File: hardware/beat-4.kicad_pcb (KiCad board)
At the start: 4 copper layers, 70 x 70 mm, 109 parts, among them J1001 SJ2-25404B-SMT-TR, J101 Cortex, J102 DX07S016JA3, J201 DX07S016JA3, J202 KitProg3, J401 WAGO 2601-1101, J402 WAGO 2601-1101, J403 WAGO 2601-1101, J404 WAGO 2601-1101, J405 WAGO 2601-1101, J406 WAGO 2601-1101, J407 WAGO 2601-1101, J408 WAGO 2601-1101, Q201 BSC010N04LS, Q202 BSC010N04LS, Q601 BSC010N04LS, Q701 BSC010N04LS, Q801 BSC010N04LS, Q901 BSC010N04LS, SW101 SKSG, SW102 SKSG, U1001 TLP2361, U101 ATSAMD51G, U102 TPS78433QWDRBRQ1, U201 CYPM1311-48LDXI, U301 TPSM33620S5QRDNRQ1, U501 BTT6010, Y101 32k768

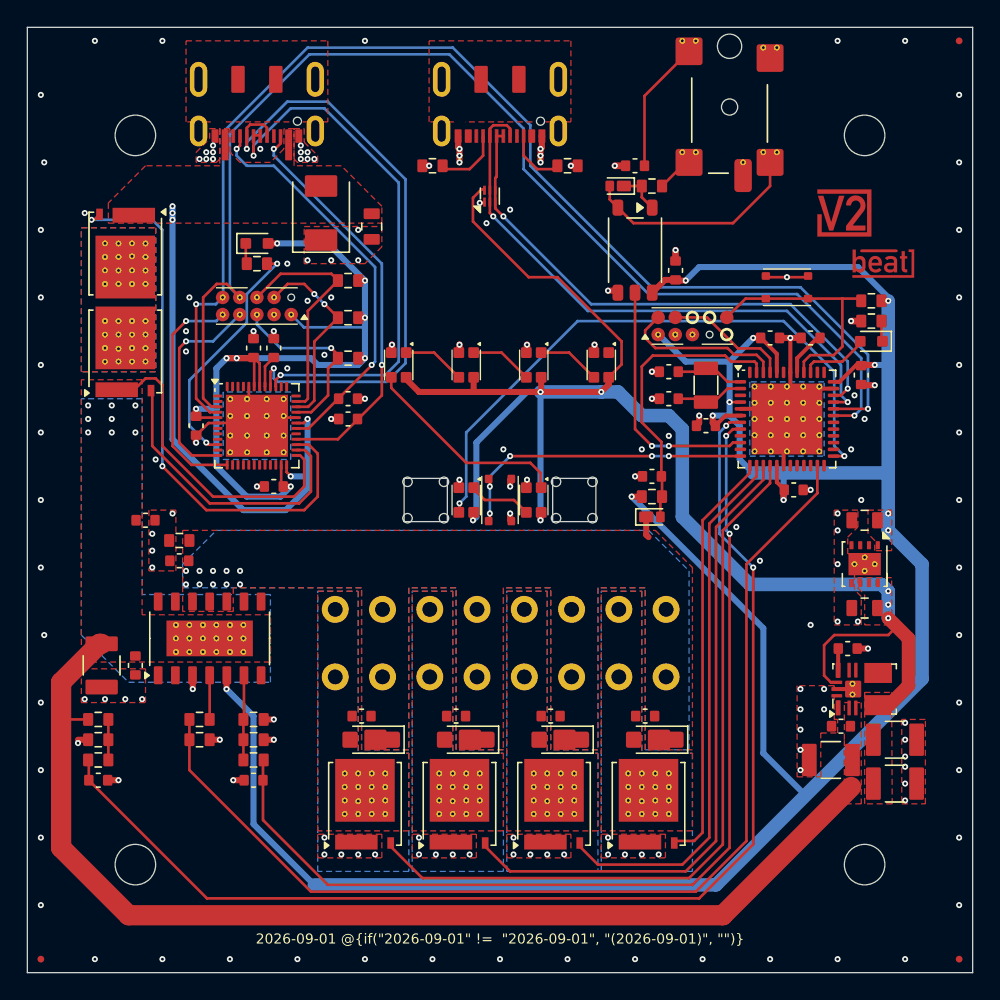
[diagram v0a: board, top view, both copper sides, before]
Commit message: Update USB-PD SWD
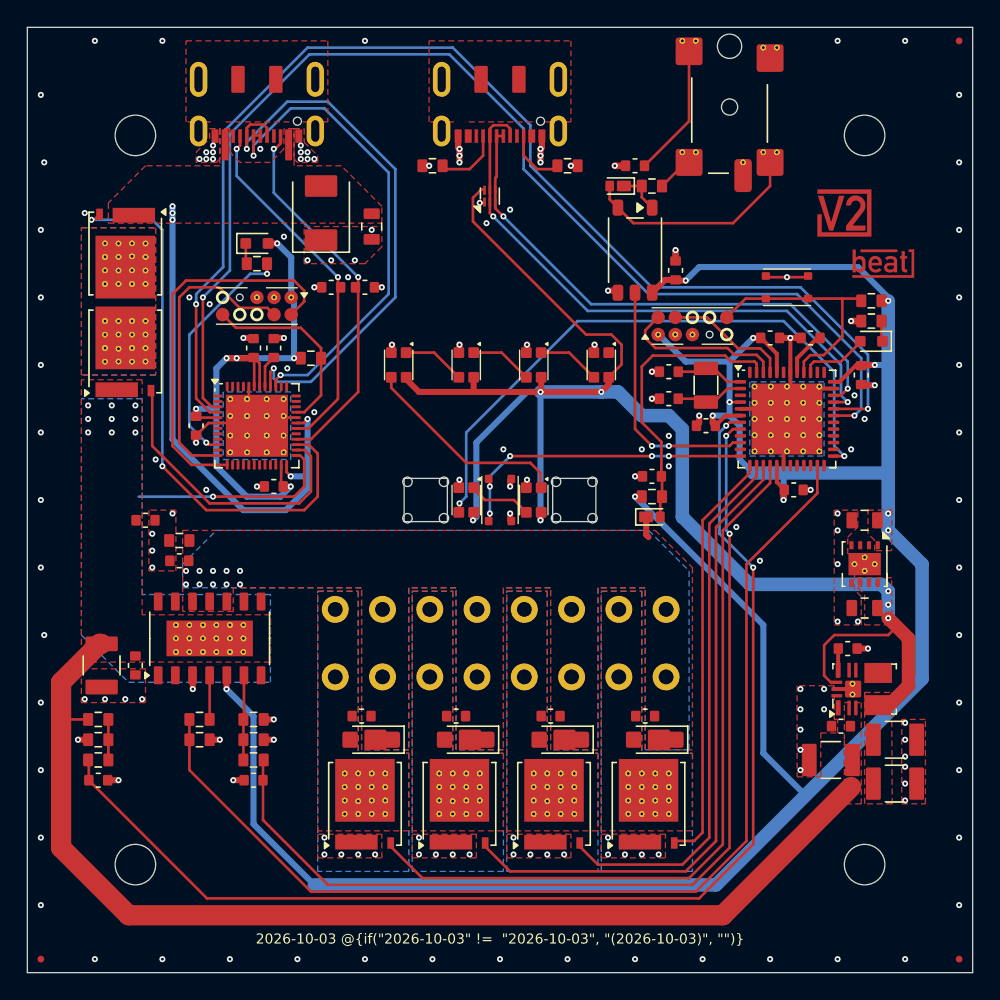
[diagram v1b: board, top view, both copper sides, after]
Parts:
- removed R203, R204: 3k9, V2_Resistor_SMD:R_1608
- J202: value KitProg3 -> Cortex; footprint V2_Connector_Debug:KitProg3 -> V2_Connector_Debug:Cortex
- moved C207 9.83 mm to (142.0, 64.2), turned to 0 degrees
- moved C208 8.34 mm to (139.5, 64.2), turned to 180 degrees
- moved R202 2.75 mm to (138.0, 69.5), turned to 180 degrees
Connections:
- J202 pad 10: /USB-PD-RX -> /Power USB/RESET
- J202 pad 4: /Power USB/SCL -> /Power USB/SWCLK
- J202 pad 5: /Power USB/RESET -> GND
- U201 pad 34: /Power USB/SCL -> unconnected-(U201-P4.0/I2C_SCL-Pad34)
- U201 pad 35: /Power USB/SDA -> unconnected-(U201-P4.1/I2C_SDA-Pad35)
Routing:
- net /Power USB/SDA: track 17.6 -> 0.00 mm
- net /Power USB/+VSYS: track 59.6 -> 42.2 mm, vias 8 -> 6
- net /Power USB/SCL: track 14.6 -> 0.00 mm, vias 2 -> 0
- net /Power USB/SWDIO: track 17.2 -> 28.5 mm, vias 1 -> 0
- net /+VSUPPLY: track 106.5 -> 99.5 mm, vias 8 -> 10
- net /Power USB/SWCLK: track 15.8 -> 22.2 mm, vias 1 -> 0
- net /Power USB/USB+: track 40.5 -> 36.5 mm
- net /Power USB/USB-: track 45.9 -> 42.0 mm
- net /Power USB/USB-CC2: track 30.2 -> 26.7 mm
- net /USB-PD-TX: track 91.1 -> 88.1 mm, vias 1 -> 2
- net /Power USB/USB-CC1: track 30.6 -> 27.9 mm
- net /USB-PD-RX: track 91.5 -> 90.7 mm
- net GND: track 48.9 -> 49.3 mm, vias 172 -> 170
- net /Power USB/RESET: track 13.8 -> 14.2 mm, vias 1 -> 0
